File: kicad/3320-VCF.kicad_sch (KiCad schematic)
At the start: 57 parts, among them J1 EuroPower_JST_3P, J2 EURO_PWR_16P, U1 AS3320, U2 TL072, U3 TL074

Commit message: schematic updated
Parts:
- removed R12: 51K, symbol Device:R
- removed R26: 240K, symbol Device:R
- removed R27: 100K, symbol Device:R
- removed R28: 68K, symbol Device:R
- removed R29: 3K, symbol Device:R
- added C14, C15: 4.7uF, symbol Device:C_Polarized
- added C16, C3: 22uF, symbol Device:C_Polarized
- added R1, R13, R21, R3: 100K, symbol Device:R
- added R14: 68K, symbol Device:R
- added R19: 240K, symbol Device:R
- added R20: 51K, symbol Device:R
- added R22: 3K, symbol Device:R
- added RV1: 2K, symbol Device:R_Potentiometer_Trim
- C1: renamed from C10; value 2.2uF -> 4.7uF
- C2: renamed from C7; value 2.2uF -> 4.7uF
- renumbered C8 to C10, C9 to C11, C1 to C12, C2 to C13, C3 to C4, C4 to C5, C5 to C6, C6 to C7, C11 to C8, C12 to C9, R9 to R10, R10 to R11, R11 to R12, R30 to R15, R13 to R16, R7 to R17, R8 to R18, R31 to R2, R16 to R23, R14 to R24, R17 to R25, R18 to R26, R15 to R27, R1 to R28, R23 to R29, R25 to R30, R21 to R31, R24 to R32, R19 to R33, R20 to R34, R22 to R35, R32 to R4, R2 to R5, R3 to R6, R4 to R7, R5 to R8, R6 to R9, RV3 to RV2, RV1 to RV3, RV2 to RV4, RV4 to RV5, RV5 to RV6, RV6 to RV7, U2 to U1, U3 to U2, U1 to U3
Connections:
- net 3320_Out4: now also C15.2; no longer C2.1
- net 3320_Vres: now also R20.2, R22.1
- net GND: now also U1.3 (+), R14.2, R21.2, R22.2, RV1.1
- net at C2.2, U1.5 (+): now also R14.1
- net at R4.1, U1.1: now also R1.2; no longer U1.2 (-)
- net at R4.2: now also C14.1; no longer C1.1
- net at C1.2: now also C14.2; no longer R5.1
- net at R2.2: now also U1.2 (-), R1.1; no longer U1.3 (+)
- net at U1.7: now also C16.2, R19.2, R20.1; no longer R15.1
- net at U1.6 (-): now also R19.1, R21.1
- net at U2.13 (-): now also R13.1, R3.2; no longer U2.14
- new net: C15.1, C2.1
- new net: C3.2, R13.2
- new net: C1.1, R5.1
- new net: R3.1, RV1.3, U2.14
- new net: R15.1, RV1.2
- new net: C16.1, C3.1
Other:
- note added: "Gain = 3.4"
- note added: "Input inverter"
- note added: "Output amplitude trim"
- note added: "Output inverter"
- note added: "Target Capacitance: 2.2uF"
- note added: "Target capacitance: 10uF"
- note added: "Target capacitance: 2.2uF"
- note removed: "Input Buffer"
- moved on the sheet: C1, C2, C4, C5, C6, C7, C8, C9, R10, R11, R12, R15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

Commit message: Added Schematic Revision 0.1.1
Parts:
- removed C14, C2: 4.7uF, symbol Device:C_Polarized
- removed C16, C3: 22uF, symbol Device:C_Polarized
- removed R1, R13, R3: 100K, symbol Device:R
- removed R4: 10K, symbol Device:R
- C1, C15: value 4.7uF -> 2.2uF
- C4, C5, C6, C7: value 330pF -> 270pF
- R19: value 240K -> 220K
- R22: value 3K -> 3K3
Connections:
- net 3320_Out4: now also C15.1; no longer C15.2
- net GND: no longer U1.3 (+)
- net at R14.1, U1.5 (+): now also C15.2
- net at C1.2: now also R20.1
- net at U1.1: now also R5.1, U1.2 (-)
- net at U2.13 (-): now also U2.14
- net at C1.1: now also R19.2, RV1.3, U1.7; no longer R5.1
- net at R2.2: now also U1.3 (+); no longer U1.2 (-)
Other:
- note added: "3340 Output DC bias: typ = 6.5V @ VCC = 15V Vin = 0V"
- note added: "9Vpp max"
- note added: "AC coupling caps can be polarized electrolytics or film caps. Make sure the polarity is right!"
- note added: "Freq CV gain Trim"
- note added: "Gain = 3.2"
- note added: "Input buffer"
- note added: "REE = (VEE-2.7)/0.08"
- note added: "Reso CV gain Trim"
- note added: "Tested good"
- note added: "The chip can surprisingly handle 10Vpp audio signals!"
- note added: "Untested"
- note added: "VppOut = VCC - 3V"
- note removed: "Gain = 3.4"
- note removed: "Input inverter"
- note removed: "Output inverter"
- note removed: "Reso Trim"
- note removed: "Target Capacitance: 2.2uF"
- note removed: "Target capacitance: 10uF"
- note removed: "Target capacitance: 2.2uF"
- moved on the sheet: C10, C11, C15, R14, R15, R2, R20, R22, R23, R24, R25, R26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

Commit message: added Schematic rev 0.1.1 pdf
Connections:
- net -12V: now also RV3.1; no longer RV3.3
- net GND: now also RV3.3; no longer RV3.1
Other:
- note added: "Op amp power and decoupling"
- note added: "Test output levels!"
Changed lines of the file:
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@@
     (stroke (width 0) (type default))
   )
-  (wire (pts (xy 249.174 142.621) (xy 249.174 143.891))
+  (wire (pts (xy 249.174 142.621) (xy 249.174 143.256))
     (stroke (width 0) (type default))
   )
@@
     (fill (type none))
   )
-  (rectangle (start 256.286 58.42) (end 346.837 118.745)
+  (rectangle (start 256.286 58.42) (end 346.837 105.029)
     (stroke (width 0) (type dash_dot))
     (fill (type none))
@@
     (effects (font (size 1.27 1.27)) (justify left bottom))
   )
+  (text "Op amp power and decoupling" (at 118.364 238.125 0)
+    (effects (font (size 1.27 1.27)) (justify left bottom))
+  )
   (text "Resonance Control Circuit" (at 16.637 180.086 0)
     (effects (font (size 2 2)) (justify left bottom))
@@
     (effects (font (size 3 3)) (justify left bottom))
   )
+  (text "Test output levels!" (at 322.326 62.992 0)
+    (effects (font (size 1.27 1.27)) (justify left bottom))
+  )
   (text "Untested" (at 16.891 181.991 0)
     (effects (font (size 1.27 1.27)) (justify left bottom))
@@
     )
   )
-  (symbol (lib_id "power:GND") (at 249.174 143.891 0) (unit 1)
+  (symbol (lib_id "power:GND") (at 249.174 143.256 0) (unit 1)
     (in_bom yes) (on_board yes) (dnp no) (fields_autoplaced)
-    (property "Reference" "#PWR016" (at 249.174 150.241 0)
+    (property "Reference" "#PWR016" (at 249.174 149.606 0)
       (effects (font (size 1.27 1.27)) hide)
     )
-    (property "Value" "GND" (at 249.174 148.336 0)
+    (property "Value" "GND" (at 249.174 147.701 0)
       (effects (font (size 1.27 1.27)))
     )
-    (property "Footprint" "" (at 249.174 143.891 0)
+    (property "Footprint" "" (at 249.174 143.256 0)
       (effects (font (size 1.27 1.27)) hide)
     )
-    (property "Datasheet" "" (at 249.174 143.891 0)
+    (property "Datasheet" "" (at 249.174 143.256 0)
       (effects (font (size 1.27 1.27)) hide)
     )
@@
   )
   (symbol (lib_id "Device:R") (at 242.951 151.13 0) (unit 1)
-    (in_bom yes) (on_board yes) (dnp no) (fields_autoplaced)
-    (property "Reference" "R28" (at 244.856 149.86 0)
+    (in_bom yes) (on_board yes) (dnp no)
+    (property "Reference" "R28" (at 244.856 150.368 0)
       (effects (font (size 1.27 1.27)) (justify left))
     )
@@
     )
   )
-  (symbol (lib_id "Device:R_Potentiometer") (at 32.258 142.621 0) (unit 1)
+  (symbol (lib_id "Device:R_Potentiometer") (at 32.258 142.621 0) (mirror x) (unit 1)
     (in_bom yes) (on_board yes) (dnp no)
-    (property "Reference" "RV3" (at 30.48 143.891 0)
+    (property "Reference" "RV3" (at 30.48 141.351 0)
       (effects (font (size 1.27 1.27)) (justify right))
     )
-    (property "Value" "100K" (at 30.48 141.351 0)
+    (property "Value" "100K" (at 30.48 143.891 0)
       (effects (font (size 1.27 1.27)) (justify right))
     )

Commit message: added schematic revision 0.1.2
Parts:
- R15: renamed from R19; value 220K -> 330K
- renumbered C15 to C1, C13 to C12, C1 to C2, C4 to C3, C5 to C4, C6 to C5, C7 to C6, C8 to C7, C9 to C8, C12 to C9, R2 to R1, R15 to R10, R14 to R11, R16 to R12, R17 to R13, R18 to R14, R21 to R16, R20 to R17, R22 to R18, R23 to R19, R5 to R2, R24 to R20, R25 to R21, R26 to R22, R28 to R23, R27 to R24, R29 to R25, R30 to R26, R31 to R27, R32 to R28, R33 to R29, R6 to R3, R34 to R30, R35 to R31, R7 to R4, R8 to R5, R9 to R6, R10 to R7, R11 to R8, R12 to R9, U3 to U2, U2 to U3
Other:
- note added: "Gain = 4.3"
- note removed: "Gain = 3.2"
- note removed: "Test output levels!"
- note removed: "Tested good"
- note removed: "Untested"

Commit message: added schem rev 0.1.3
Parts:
- added J3: Sig In, DIYSynthMNL:AudioJack_3.5mm_long_pads, symbol DIYSynthMNL:PJ3001F
- added J4: Sig Out, DIYSynthMNL:AudioJack_3.5mm_long_pads, symbol DIYSynthMNL:PJ3001F
- added J5: ResCv, DIYSynthMNL:AudioJack_3.5mm_long_pads, symbol DIYSynthMNL:PJ3001F
- added J6: FreqCv, DIYSynthMNL:AudioJack_3.5mm_long_pads, symbol DIYSynthMNL:PJ3001F
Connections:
- net Audio_in: now also J3.T
- net Audio_out: now also J4.T
- net Freq_CV_in: now also J6.T
- net GND: now also J3.S, J4.S, J5.S, J6.S
- net Reso_CV_in: now also J5.T
- no-connect marks 6 -> 10
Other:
- moved on the sheet: R19, R20, R21, R22, R24, R25, R26, R27, R28, R29, R30, R31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

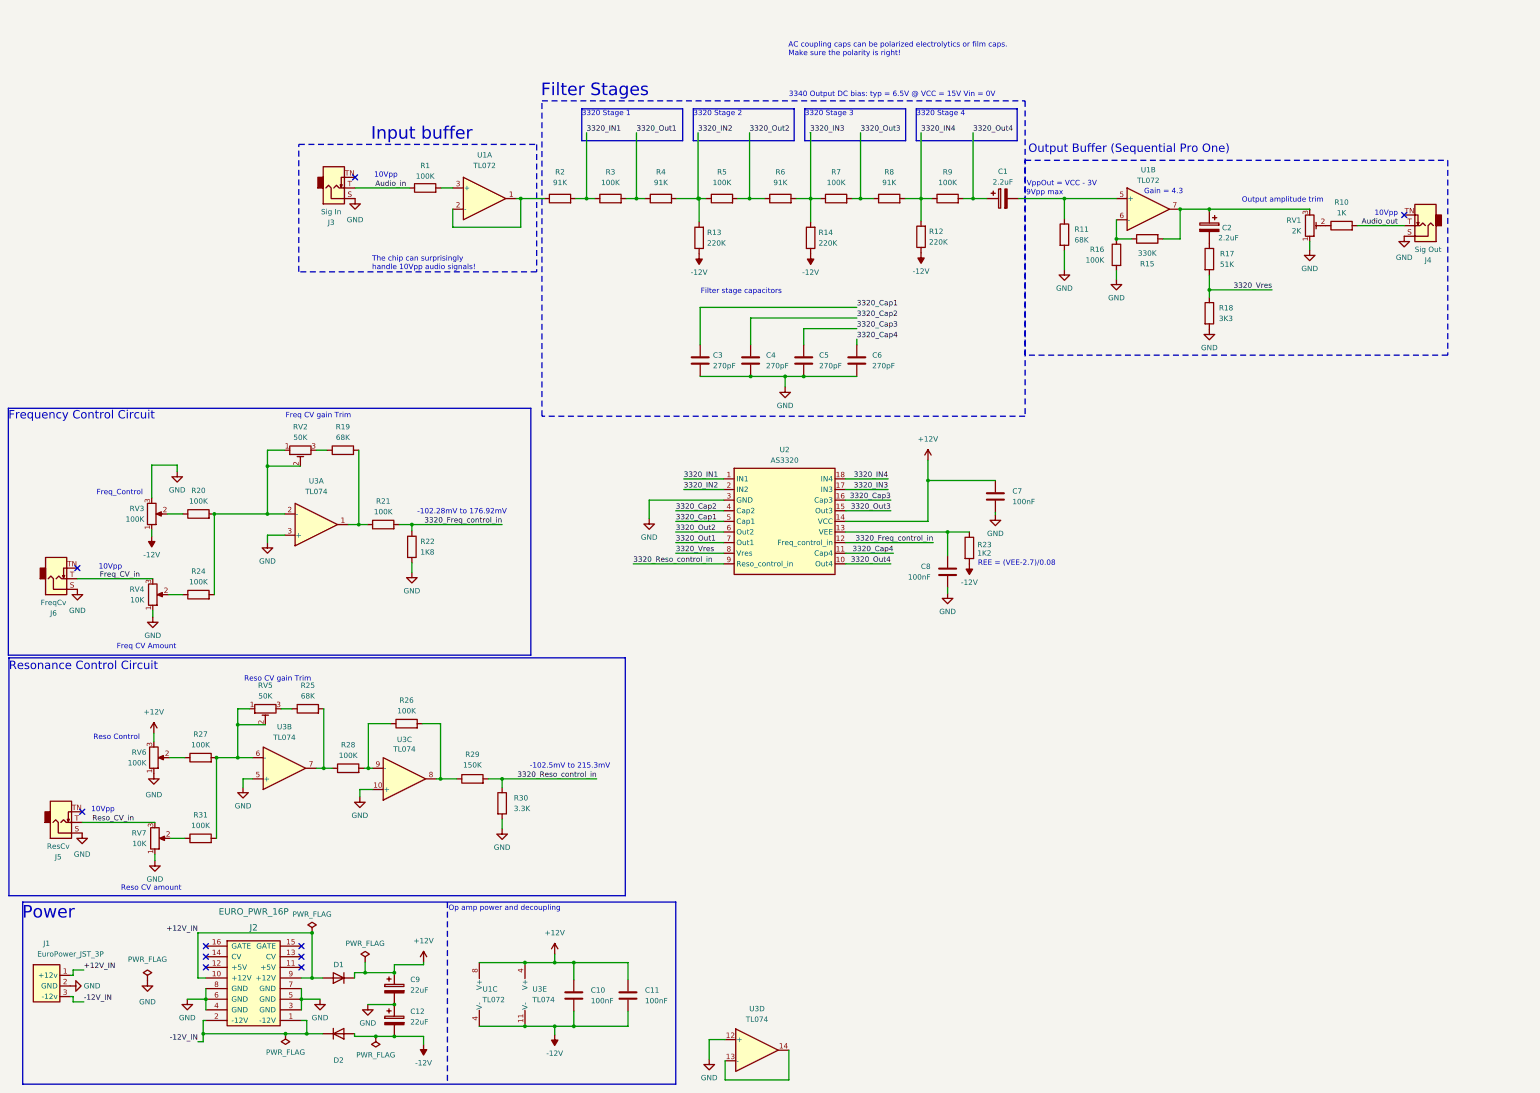
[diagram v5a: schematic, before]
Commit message: assigned footprints
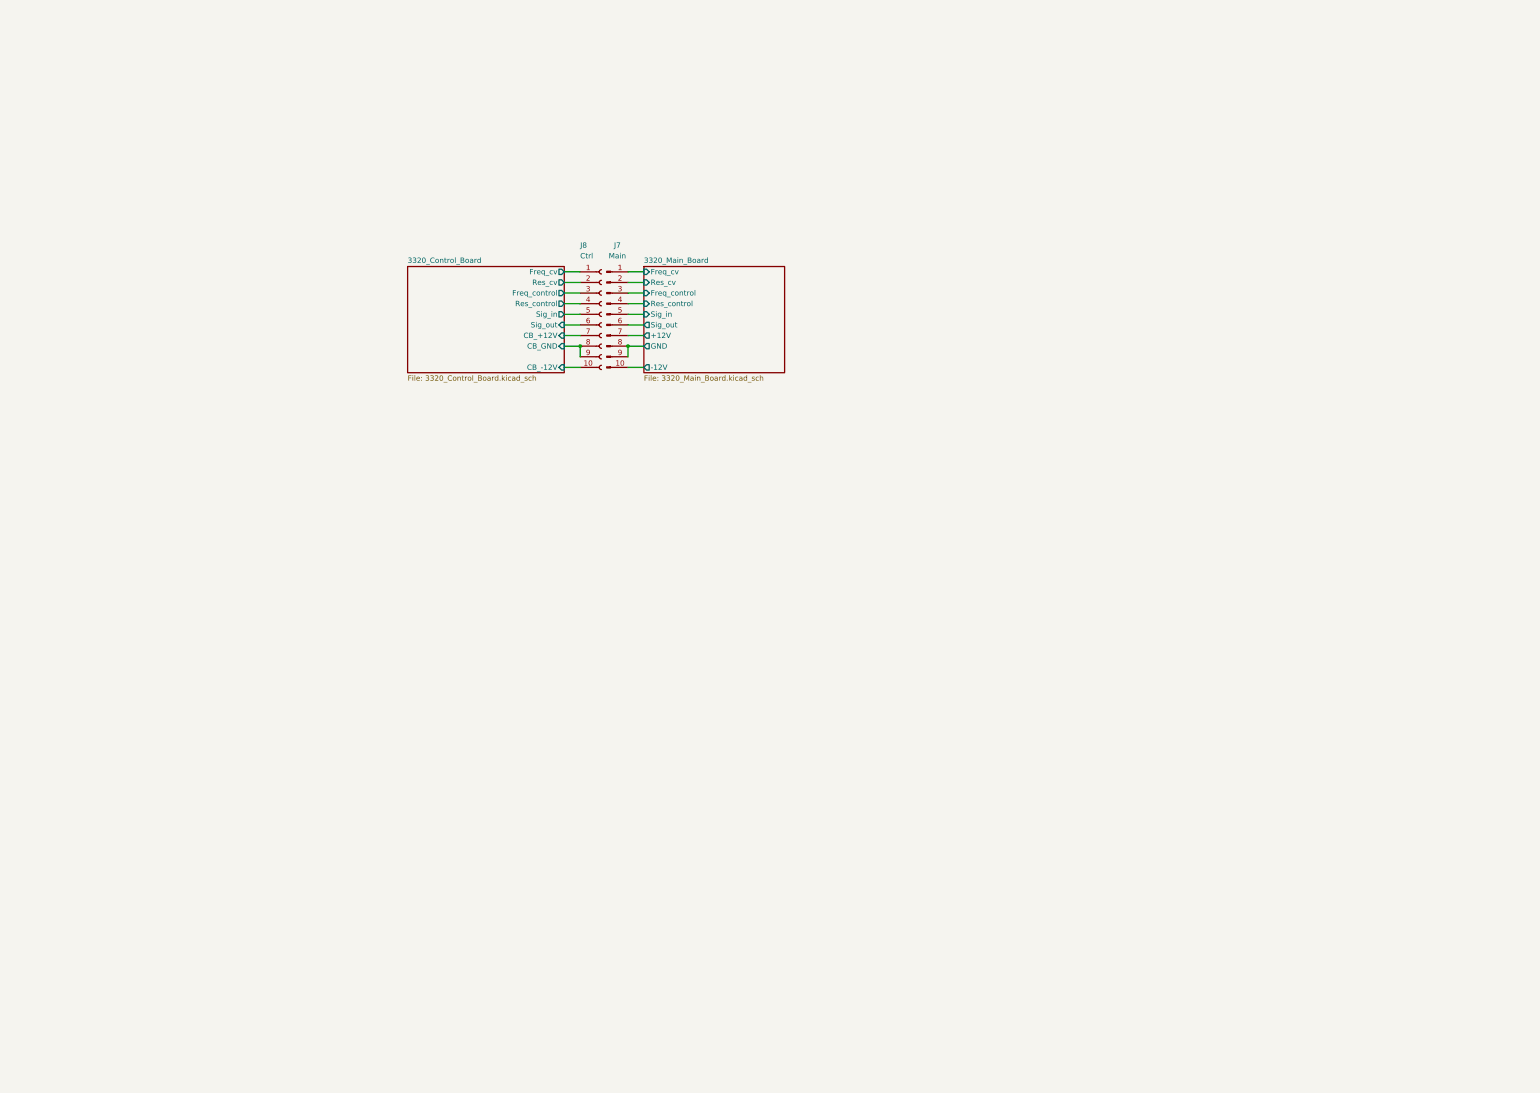
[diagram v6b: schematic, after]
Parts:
- removed C1, C2: 2.2uF, symbol Device:C_Polarized
- removed C10, C11, C7, C8: 100nF, symbol Device:C
- removed C12, C9: 22uF, DIYSynthMNL:CP_Radial_D4.0mm_P1.50mm, symbol Device:C_Polarized
- removed C3, C4, C5, C6: 270pF, symbol Device:C
- removed D1, D2: ~, DIYSynthMNL:D_DO-41_SOD81_P7.62mm_Horizontal_BigPads, symbol Device:D
- removed J1: EuroPower_JST_3P, DIYSynthMNL:Eurorack_power_jst_3P, symbol DIYSynthMNL:JST_Eurorack_power_3P
- removed J2: EURO_PWR_16P, DIYSynthMNL:IDC-Header_2x08_P2.54mm_Vertical, symbol DIYSynthMNL:EURO_PWR_16_PIN
- removed J3: Sig In, DIYSynthMNL:AudioJack_3.5mm_long_pads, symbol DIYSynthMNL:PJ3001F
- removed J4: Sig Out, DIYSynthMNL:AudioJack_3.5mm_long_pads, symbol DIYSynthMNL:PJ3001F
- removed J5: ResCv, DIYSynthMNL:AudioJack_3.5mm_long_pads, symbol DIYSynthMNL:PJ3001F
- removed J6: FreqCv, DIYSynthMNL:AudioJack_3.5mm_long_pads, symbol DIYSynthMNL:PJ3001F
- removed R1, R16, R20, R21, R24, R26, R27, R28, R3, R31, R5, R7, R9: 100K, symbol Device:R
- removed R10: 1K, symbol Device:R
- removed R11, R19, R25: 68K, symbol Device:R
- removed R12, R13, R14: 220K, symbol Device:R
- removed R15: 330K, symbol Device:R
- removed R17: 51K, symbol Device:R
- removed R18: 3K3, symbol Device:R
- removed R2, R4, R6, R8: 91K, symbol Device:R
- removed R22: 1K8, symbol Device:R
- removed R23: 1K2, symbol Device:R
- removed R29: 150K, symbol Device:R
- removed R30: 3.3K, symbol Device:R
- removed RV1: 2K, symbol Device:R_Potentiometer_Trim
- removed RV2, RV5: 50K, symbol Device:R_Potentiometer_Trim
- removed RV3, RV6: 100K, symbol Device:R_Potentiometer
- removed RV4, RV7: 10K, symbol Device:R_Potentiometer
- removed U1: TL072, symbol Amplifier_Operational:TL072
- removed U2: AS3320, symbol DIYSynthMNL:AS3320
- removed U3: TL074, symbol Amplifier_Operational:TL074
- added J7: Main, Connector_PinHeader_2.54mm:PinHeader_1x10_P2.54mm_Vertical, symbol Connector:Conn_01x10_Pin
- added J8: Ctrl, Connector_PinSocket_2.54mm:PinSocket_1x10_P2.54mm_Vertical, symbol Connector:Conn_01x10_Socket
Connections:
- new net 3320_Control_Board/CB_+12V: J8.7 (Pin_7)
- new net 3320_Control_Board/CB_-12V: J8.10 (Pin_10)
- new net 3320_Control_Board/CB_GND: J8.8 (Pin_8), J8.9 (Pin_9)
- new net 3320_Control_Board/Freq_control: J8.3 (Pin_3)
- new net 3320_Control_Board/Freq_cv: J8.1 (Pin_1)
- new net 3320_Control_Board/Res_control: J8.4 (Pin_4)
- new net 3320_Control_Board/Res_cv: J8.2 (Pin_2)
- new net 3320_Control_Board/Sig_in: J8.5 (Pin_5)
- new net 3320_Control_Board/Sig_out: J8.6 (Pin_6)
- new net 3320_Main_Board/+12V: J7.7 (Pin_7)
- new net 3320_Main_Board/-12V: J7.10 (Pin_10)
- new net 3320_Main_Board/Freq_control: J7.3 (Pin_3)
- new net 3320_Main_Board/Freq_cv: J7.1 (Pin_1)
- new net 3320_Main_Board/GND: J7.8 (Pin_8), J7.9 (Pin_9)
- new net 3320_Main_Board/Res_control: J7.4 (Pin_4)
- new net 3320_Main_Board/Res_cv: J7.2 (Pin_2)
- new net 3320_Main_Board/Sig_in: J7.5 (Pin_5)
- new net 3320_Main_Board/Sig_out: J7.6 (Pin_6)
- no-connect marks 10 -> 0
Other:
- added sheet 3320_Control_Board (3320_Control_Board.kicad_sch)
- added sheet 3320_Main_Board (3320_Main_Board.kicad_sch)
- note removed: "-102.28mV to 176.92mV"
- note removed: "-102.5mV to 215.3mV"
- note removed: "10Vpp"
- note removed: "3320 Stage 1"
- note removed: "3320 Stage 2"
- note removed: "3320 Stage 3"
- note removed: "3320 Stage 4"
- note removed: "3340 Output DC bias: typ = 6.5V @ VCC = 15V Vin = 0V"
- note removed: "9Vpp max"
- note removed: "AC coupling caps can be polarized electrolytics or film caps. Make sure the polarity is right!"
- note removed: "Filter Stages"
- note removed: "Filter stage capacitors"
- note removed: "Freq CV Amount"
- note removed: "Freq CV gain Trim"
- note removed: "Freq_Control"
- note removed: "Frequency Control Circuit"
- note removed: "Gain = 4.3"
- note removed: "Input buffer"
- note removed: "Op amp power and decoupling"
- note removed: "Output Buffer (Sequential Pro One)"
- note removed: "Output amplitude trim"
- note removed: "Power"
- note removed: "REE = (VEE-2.7)/0.08"
- note removed: "Reso CV amount"
- note removed: "Reso CV gain Trim"
- note removed: "Reso Control"
- note removed: "Resonance Control Circuit"
- note removed: "The chip can surprisingly handle 10Vpp audio signals!"
- note removed: "VppOut = VCC - 3V"
